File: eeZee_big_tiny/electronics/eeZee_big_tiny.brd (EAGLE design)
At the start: 36.3 x 16.3 mm, 11 parts, among them IC1 ATtiny2313/4313, J2 avrisp, Q1 16MHz

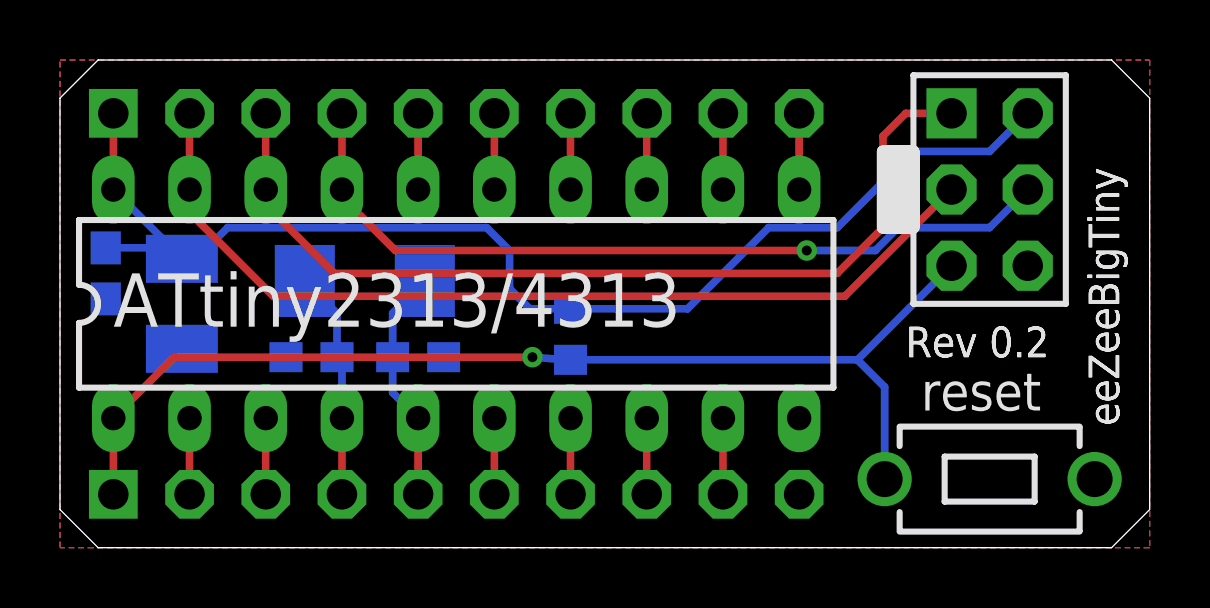
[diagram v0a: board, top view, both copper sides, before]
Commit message: Changed spaces to 10mil/8mil, relocated trace
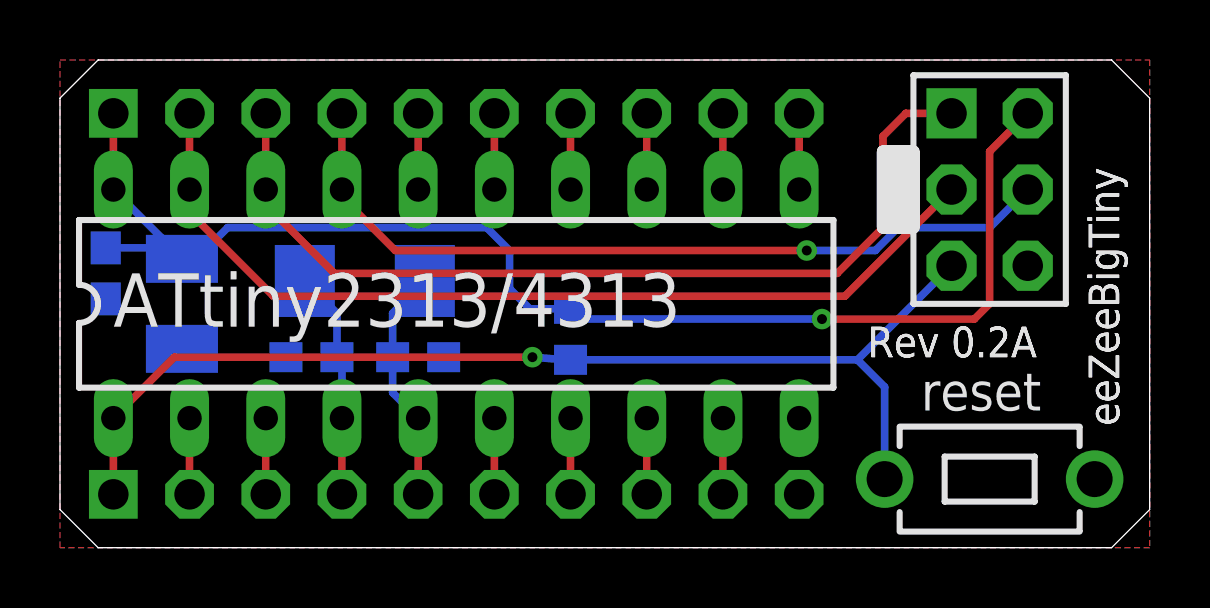
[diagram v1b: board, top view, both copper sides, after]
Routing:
- net VCC: track 41.7 -> 45.0 mm, vias 0 -> 1
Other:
- board text added: "Rev 0.2A"
- board text removed: "Rev 0.2"
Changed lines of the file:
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@@
 <layer number="19" name="Unrouted" color="6" fill="1" visible="yes" active="yes"/>
 <layer number="20" name="Dimension" color="15" fill="1" visible="yes" active="yes"/>
-<layer number="21" name="tPlace" color="7" fill="1" visible="no" active="yes"/>
-<layer number="22" name="bPlace" color="7" fill="1" visible="no" active="yes"/>
-<layer number="23" name="tOrigins" color="15" fill="1" visible="no" active="yes"/>
-<layer number="24" name="bOrigins" color="15" fill="1" visible="no" active="yes"/>
-<layer number="25" name="tNames" color="7" fill="1" visible="no" active="yes"/>
-<layer number="26" name="bNames" color="7" fill="1" visible="no" active="yes"/>
-<layer number="27" name="tValues" color="7" fill="1" visible="no" active="yes"/>
-<layer number="28" name="bValues" color="7" fill="1" visible="no" active="yes"/>
+<layer number="21" name="tPlace" color="7" fill="1" visible="yes" active="yes"/>
+<layer number="22" name="bPlace" color="7" fill="1" visible="yes" active="yes"/>
+<layer number="23" name="tOrigins" color="15" fill="1" visible="yes" active="yes"/>
+<layer number="24" name="bOrigins" color="15" fill="1" visible="yes" active="yes"/>
+<layer number="25" name="tNames" color="7" fill="1" visible="yes" active="yes"/>
+<layer number="26" name="bNames" color="7" fill="1" visible="yes" active="yes"/>
+<layer number="27" name="tValues" color="7" fill="1" visible="yes" active="yes"/>
+<layer number="28" name="bValues" color="7" fill="1" visible="yes" active="yes"/>
 <layer number="29" name="tStop" color="7" fill="3" visible="yes" active="yes"/>
 <layer number="30" name="bStop" color="7" fill="6" visible="yes" active="yes"/>
@@
 <vertex x="21.8701875" y="7.324015625"/>
 </polygon>
-<text x="28.194" y="6.35" size="1.016" layer="25" font="vector" ratio="16">Rev 0.2</text>
+<text x="26.924" y="6.35" size="1.016" layer="25" font="vector" ratio="16">Rev 0.2A</text>
 <text x="35.306" y="4.064" size="1.016" layer="25" font="vector" ratio="16" rot="R90">eeZeeBigTiny</text>
 <wire x1="32.434809375" y1="2.363190625" x2="29.541190625" y2="2.363190625" width="0.2032" layer="22"/>
@@
 <vertex x="21.8701875" y="7.3240125"/>
 </polygon>
-<text x="28.194" y="6.35" size="1.016" layer="121" font="vector" ratio="20">Rev 0.2</text>
+<text x="26.924" y="6.35" size="1.016" layer="121" font="vector" ratio="20">Rev 0.2A</text>
 <text x="35.306" y="4.064" size="1.016" layer="121" font="vector" ratio="20" rot="R90">eeZeeBigTiny</text>
 <text x="34.544" y="4.318" size="0.8128" layer="122" font="vector" ratio="25" rot="MR90">bot-thoughts.com</text>
@@
 </class>
 </classes>
-<designrules name="default *">
+<designrules name="LaenPCBOrder *">
 <description language="de">&lt;b&gt;EAGLE Design Rules&lt;/b&gt;
 &lt;p&gt;
@@
 <param name="mtCopper" value="0.0356mm 0.0356mm 0.0356mm 0.0356mm 0.0356mm 0.0356mm 0.0356mm 0.0356mm 0.0356mm 0.0356mm 0.0356mm 0.0356mm 0.0356mm 0.0356mm 0.0356mm 0.0356mm"/>
 <param name="mtIsolate" value="1.5011mm 0.1499mm 0.2007mm 0.1499mm 0.2007mm 0.1499mm 0.2007mm 0.1499mm 0.2007mm 0.1499mm 0.2007mm 0.1499mm 0.2007mm 0.1499mm 0.2007mm"/>
-<param name="mdWireWire" value="6mil"/>
-<param name="mdWirePad" value="6mil"/>
-<param name="mdWireVia" value="6mil"/>
-<param name="mdPadPad" value="6mil"/>
-<param name="mdPadVia" value="6mil"/>
-<param name="mdViaVia" value="6mil"/>
-<param name="mdSmdPad" value="6mil"/>
-<param name="mdSmdVia" value="6mil"/>
-<param name="mdSmdSmd" value="6mil"/>
+<param name="mdWireWire" value="10mil"/>
+<param name="mdWirePad" value="10mil"/>
+<param name="mdWireVia" value="10mil"/>
+<param name="mdPadPad" value="10mil"/>
+<param name="mdPadVia" value="10mil"/>
+<param name="mdViaVia" value="10mil"/>
+<param name="mdSmdPad" value="0mil"/>
+<param name="mdSmdVia" value="0mil"/>
+<param name="mdSmdSmd" value="8mil"/>
 <param name="mdViaViaSameLayer" value="8mil"/>
 <param name="mnLayersViaInSmd" value="2"/>
 <param name="mdCopperDimension" value="10mil"/>
-<param name="mdDrill" value="6mil"/>
+<param name="mdDrill" value="10mil"/>
 <param name="mdSmdStop" value="0mil"/>
 <param name="msWidth" value="6mil"/>
@@
 <param name="msMicroVia" value="13mil"/>
 <param name="msBlindViaRatio" value="0.5"/>
-<param name="rvPadTop" value="0.25"/>
+<param name="rvPadTop" value="0.3"/>
 <param name="rvPadInner" value="0.25"/>
-<param name="rvPadBottom" value="0.25"/>
+<param name="rvPadBottom" value="0.3"/>
 <param name="rvViaOuter" value="0.25"/>
 <param name="rvViaInner" value="0.25"/>
 <param name="rvMicroViaOuter" value="0.25"/>
 <param name="rvMicroViaInner" value="0.25"/>
-<param name="rlMinPadTop" value="12mil"/>
+<param name="rlMinPadTop" value="7mil"/>
 <param name="rlMaxPadTop" value="20mil"/>
 <param name="rlMinPadInner" value="7mil"/>
 <param name="rlMaxPadInner" value="20mil"/>
-<param name="rlMinPadBottom" value="12mil"/>
+<param name="rlMinPadBottom" value="7mil"/>
 <param name="rlMaxPadBottom" value="20mil"/>
 <param name="rlMinViaOuter" value="7mil"/>
@@
 <param name="psTop" value="1"/>
 <param name="psBottom" value="1"/>
-<param name="psFirst" value="-1"/>
-<param name="psElongationLong" value="60"/>
-<param name="psElongationOffset" value="60"/>
+<param name="psFirst" value="1"/>
+<param name="psElongationLong" value="100"/>
+<param name="psElongationOffset" value="100"/>
 <param name="mvStopFrame" value="1"/>
 <param name="mvCreamFrame" value="0"/>
-<param name="mlMinStopFrame" value="4mil"/>
-<param name="mlMaxStopFrame" value="4mil"/>
+<param name="mlMinStopFrame" value="3mil"/>
+<param name="mlMaxStopFrame" value="3mil"/>
 <param name="mlMinCreamFrame" value="0mil"/>
 <param name="mlMaxCreamFrame" value="0mil"/>
-<param name="mlViaStopLimit" value="0mil"/>
+<param name="mlViaStopLimit" value="20mil"/>
 <param name="srRoundness" value="0"/>
 <param name="srMinRoundness" value="0mil"/>
@@
 <wire x1="1.524" y1="9.994" x2="3.698" y2="9.994" width="0.254" layer="16"/>
 <wire x1="3.698" y1="9.994" x2="4.064" y2="9.628" width="0.254" layer="16"/>
-<wire x1="17.018" y1="7.962" x2="20.916" y2="7.962" width="0.254" layer="16"/>
-<wire x1="20.916" y1="7.962" x2="23.622" y2="10.668" width="0.254" layer="16"/>
-<wire x1="23.622" y1="10.668" x2="25.908" y2="10.668" width="0.254" layer="16"/>
-<wire x1="25.908" y1="10.668" x2="28.448" y2="13.208" width="0.254" layer="16"/>
-<wire x1="28.448" y1="13.208" x2="30.988" y2="13.208" width="0.254" layer="16"/>
-<wire x1="30.988" y1="13.208" x2="32.258" y2="14.478" width="0.254" layer="16"/>
+<wire x1="17.018" y1="7.962" x2="17.018" y2="7.874" width="0.254" layer="16"/>
+<wire x1="17.018" y1="7.874" x2="17.272" y2="7.62" width="0.254" layer="16"/>
+<wire x1="17.272" y1="7.62" x2="25.4" y2="7.62" width="0.254" layer="16"/>
+<via x="25.4" y="7.62" extent="1-16" drill="0.3302"/>
+<wire x1="25.4" y1="7.62" x2="30.48" y2="7.62" width="0.254" layer="1"/>
+<wire x1="30.48" y1="7.62" x2="30.988" y2="8.128" width="0.254" layer="1"/>
+<wire x1="30.988" y1="8.128" x2="30.988" y2="13.208" width="0.254" layer="1"/>
+<wire x1="30.988" y1="13.208" x2="32.258" y2="14.478" width="0.254" layer="1"/>
 </signal>
 <signal name="!RESET">
